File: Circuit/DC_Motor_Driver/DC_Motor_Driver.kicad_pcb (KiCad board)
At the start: 2 copper layers, 54.4 x 18.8 mm, 13 parts, among them Q1 S8050, Q2 S8050, Q3 S8550, Q4 S8050, Q5 IRF540N

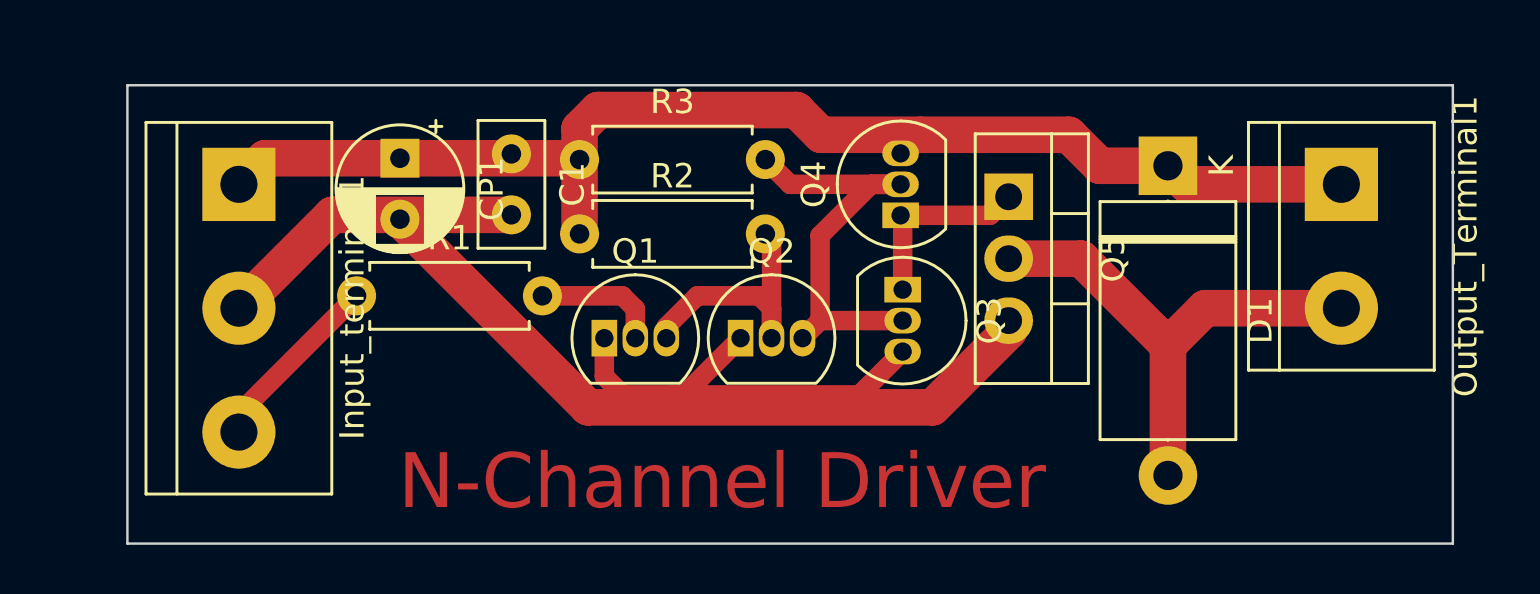
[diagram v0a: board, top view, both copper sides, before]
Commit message: Fixed DC Motor Circuit and discovered fatal design flaw in PWM demultiplexer
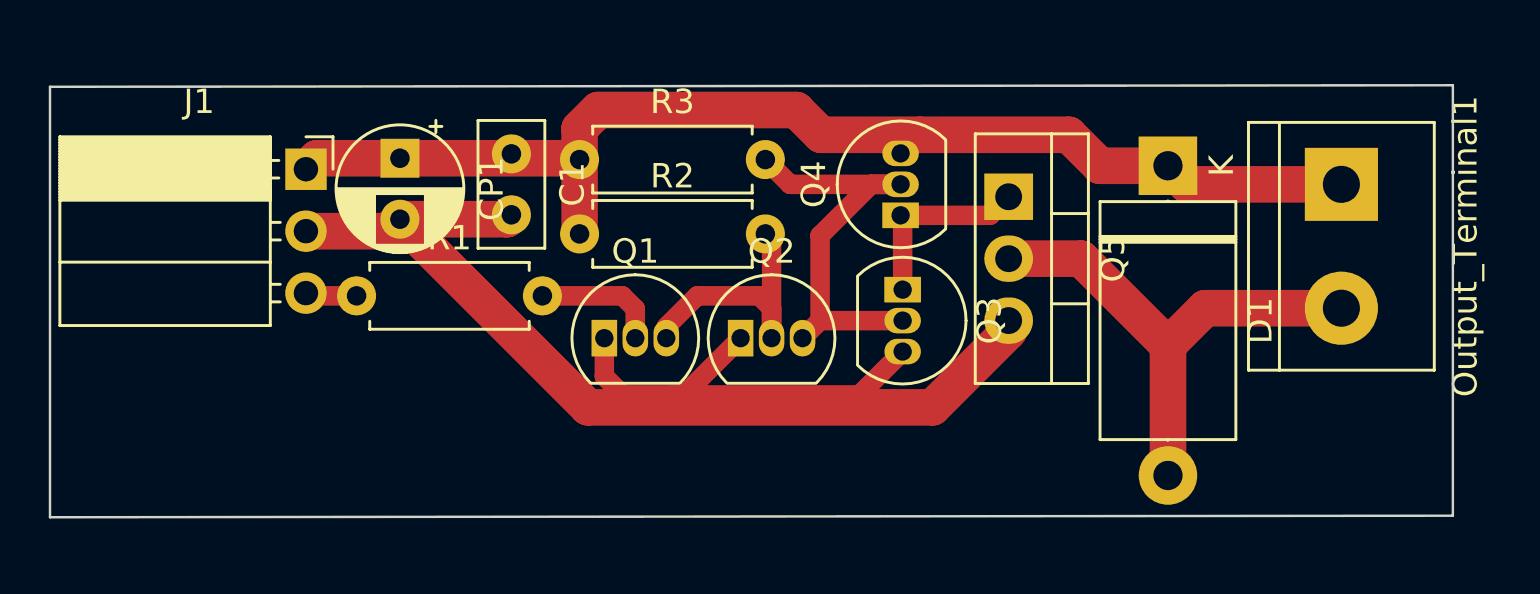
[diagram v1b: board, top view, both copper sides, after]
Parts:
- removed Input_terminal1: Screw_Terminal_01x03, TerminalBlock:TerminalBlock_bornier-3_P5.08mm
- added J1: Conn_01x03_Socket, Connector_PinSocket_2.54mm:PinSocket_1x03_P2.54mm_Horizontal, F.Cu at (20.5, -16.9)
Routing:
- net Control_Signal: track 7.59 -> 2.12 mm
- net GND: track 61.3 -> 57.2 mm
- net +12V: track 52.7 -> 49.7 mm
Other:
- board size 54.4 x 18.8 mm -> 57.5 x 17.7 mm
- board text removed: "N-Channel Driver"

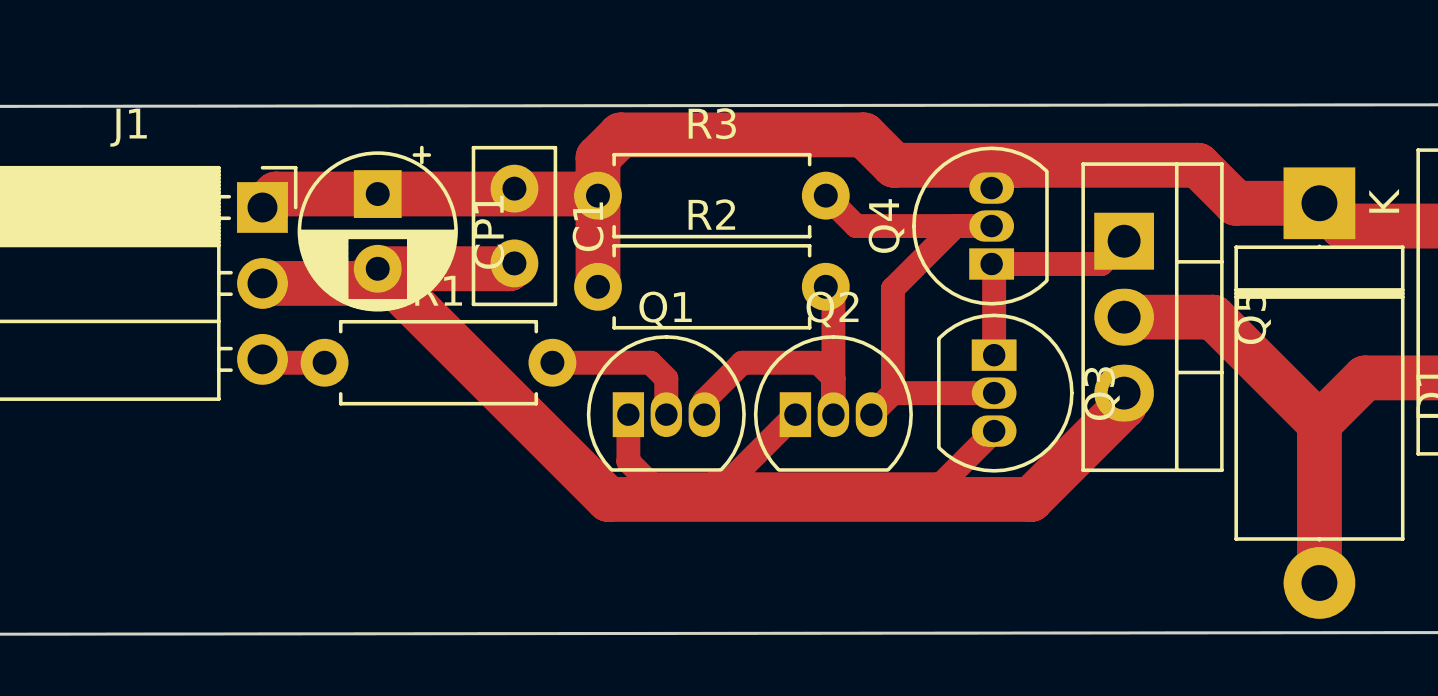
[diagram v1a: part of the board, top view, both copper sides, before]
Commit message: Implemented Isolators in PWM Mutliplexer
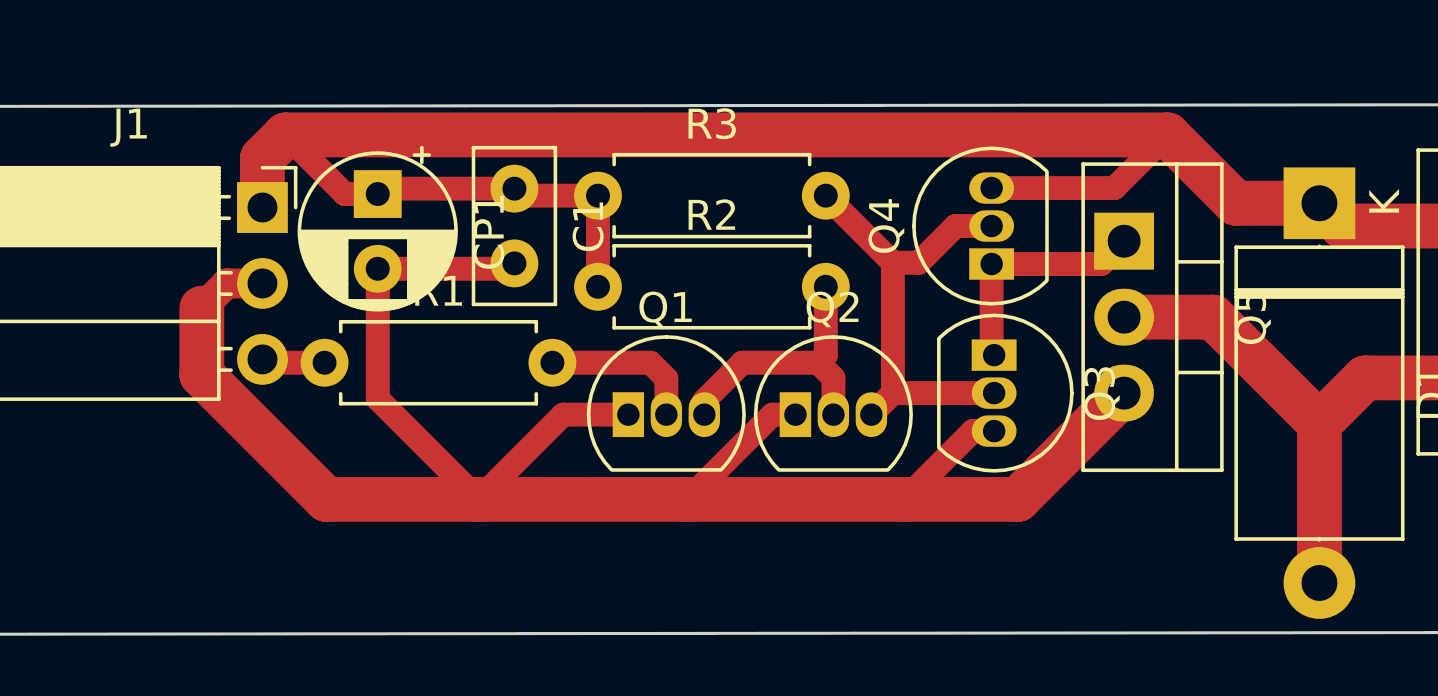
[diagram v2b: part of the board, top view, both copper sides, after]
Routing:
- net +12V: track 49.7 -> 67.2 mm
- net GND: track 57.2 -> 67.3 mm
- net Net-(Q2-C): track 18.0 -> 15.7 mm
- net Net-(Q1-C): track 11.1 -> 9.39 mm
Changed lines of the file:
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@@
   (gr_line (start 10.033 -2.6035) (end 10.033 -20.2565)
     (stroke (width 0.1) (type solid)) (layer "Edge.Cuts"))
-  (segment (start 53.086 -17.018) (end 51.816 -18.288) (width 1.5) (layer "F.Cu") (net 1))
-  (segment (start 31.75 -17.272) (end 31.75 -14.224) (width 1.5) (layer "F.Cu") (net 1))
-  (segment (start 44.916 -17.526) (end 44.958 -17.526) (width 0.8) (layer "F.Cu") (net 1))
-  (segment (start 31.75 -18.542) (end 31.75 -17.272) (width 1.5) (layer "F.Cu") (net 1))
-  (segment (start 51.816 -18.288) (end 45.72 -18.288) (width 1.5) (layer "F.Cu") (net 1))
-  (segment (start 40.64 -19.304) (end 32.512 -19.304) (width 1.5) (layer "F.Cu") (net 1))
-  (segment (start 44.958 -17.526) (end 45.72 -18.288) (width 0.8) (layer "F.Cu") (net 1))
-  (segment (start 24.384 -17.326448) (end 31.695552 -17.326448) (width 1.5) (layer "F.Cu") (net 1))
+  (segment (start 50.8 -19.304) (end 21.304 -19.304) (width 1.5) (layer "F.Cu") (net 1))
+  (segment (start 28.956 -17.506) (end 24.563552 -17.506) (width 0.8) (layer "F.Cu") (net 1))
+  (segment (start 24.563552 -17.506) (end 24.384 -17.326448) (width 0.8) (layer "F.Cu") (net 1))
+  (segment (start 44.916 -17.526) (end 44.778 -17.526) (width 0.8) (layer "F.Cu") (net 1))
+  (segment (start 44.916 -17.526) (end 49.022 -17.526) (width 0.8) (layer "F.Cu") (net 1))
+  (segment (start 31.75 -14.224) (end 31.75 -17.272) (width 0.8) (layer "F.Cu") (net 1))
   (segment (start 62.992 -16.256) (end 56.642 -16.256) (width 1.5) (layer "F.Cu") (net 1))
-  (segment (start 41.656 -18.288) (end 40.64 -19.304) (width 1.5) (layer "F.Cu") (net 1))
-  (segment (start 45.72 -18.288) (end 41.656 -18.288) (width 1.5) (layer "F.Cu") (net 1))
+  (segment (start 28.776448 -17.326448) (end 28.956 -17.506) (width 0.8) (layer "F.Cu") (net 1))
+  (segment (start 24.384 -17.326448) (end 23.281552 -17.326448) (width 0.8) (layer "F.Cu") (net 1))
+  (segment (start 55.88 -17.018) (end 53.086 -17.018) (width 1.5) (layer "F.Cu") (net 1))
+  (segment (start 23.281552 -17.326448) (end 21.304 -19.304) (width 0.8) (layer "F.Cu") (net 1))
+  (segment (start 31.75 -17.272) (end 29.19 -17.272) (width 0.8) (layer "F.Cu") (net 1))
+  (segment (start 49.022 -17.526) (end 50.8 -19.304) (width 0.8) (layer "F.Cu") (net 1))
   (segment (start 56.642 -16.256) (end 55.88 -17.018) (width 1.5) (layer "F.Cu") (net 1))
-  (segment (start 55.88 -17.018) (end 53.086 -17.018) (width 1.5) (layer "F.Cu") (net 1))
-  (segment (start 20.979448 -17.326448) (end 20.529 -16.876) (width 1.5) (layer "F.Cu") (net 1))
-  (segment (start 24.384 -17.326448) (end 20.979448 -17.326448) (width 1.5) (layer "F.Cu") (net 1))
-  (segment (start 31.695552 -17.326448) (end 31.75 -17.272) (width 1.5) (layer "F.Cu") (net 1))
-  (segment (start 32.512 -19.304) (end 31.75 -18.542) (width 1.5) (layer "F.Cu") (net 1))
-  (segment (start 43.222 -7.62) (end 45 -9.398) (width 0.8) (layer "F.Cu") (net 2))
-  (segment (start 23.893552 -14.336) (end 24.384 -14.826448) (width 1.5) (layer "F.Cu") (net 2))
-  (segment (start 28.776448 -14.826448) (end 28.956 -15.006) (width 1.5) (layer "F.Cu") (net 2))
-  (segment (start 32.766 -9.948) (end 32.766 -8.382) (width 0.8) (layer "F.Cu") (net 2))
-  (segment (start 24.384 -14.826448) (end 32.098448 -7.112) (width 1.5) (layer "F.Cu") (net 2))
-  (segment (start 35.56 -7.62) (end 36.026 -7.62) (width 0.8) (layer "F.Cu") (net 2))
-  (segment (start 36.026 -7.62) (end 38.354 -9.948) (width 0.8) (layer "F.Cu") (net 2))
-  (segment (start 33.528 -7.62) (end 35.56 -7.62) (width 0.8) (layer "F.Cu") (net 2))
-  (segment (start 46.228 -7.112) (end 49.347 -10.231) (width 1.5) (layer "F.Cu") (net 2))
-  (segment (start 32.766 -8.382) (end 33.528 -7.62) (width 0.8) (layer "F.Cu") (net 2))
-  (segment (start 49.347 -10.231) (end 49.347 -10.668) (width 1.5) (layer "F.Cu") (net 2))
-  (segment (start 32.098448 -7.112) (end 46.228 -7.112) (width 1.5) (layer "F.Cu") (net 2))
-  (segment (start 24.384 -14.826448) (end 28.776448 -14.826448) (width 1.5) (layer "F.Cu") (net 2))
-  (segment (start 20.529 -14.336) (end 23.893552 -14.336) (width 1.5) (layer "F.Cu") (net 2))
-  (segment (start 35.56 -7.62) (end 43.222 -7.62) (width 0.8) (layer "F.Cu") (net 2))
+  (segment (start 29.19 -17.272) (end 28.956 -17.506) (width 0.8) (layer "F.Cu") (net 1))
+  (segment (start 20.529 -16.876) (end 20.529 -18.529) (width 1.5) (layer "F.Cu") (net 1))
+  (segment (start 20.529 -18.529) (end 21.304 -19.304) (width 1.5) (layer "F.Cu") (net 1))
+  (segment (start 53.086 -17.018) (end 50.8 -19.304) (width 1.5) (layer "F.Cu") (net 1))
+  (segment (start 30.586 -9.948) (end 27.75 -7.112) (width 0.8) (layer "F.Cu") (net 2))
+  (segment (start 49.347 -10.668) (end 45.791 -7.112) (width 1.5) (layer "F.Cu") (net 2))
+  (segment (start 22.667415 -7.112) (end 27.75 -7.112) (width 1.5) (layer "F.Cu") (net 2))
+  (segment (start 18.5 -13.509081) (end 18.5 -11.279415) (width 1.5) (layer "F.Cu") (net 2))
+  (segment (start 27.75 -7.112) (end 34.75 -7.112) (width 1.5) (layer "F.Cu") (net 2))
+  (segment (start 45.791 -7.112) (end 42 -7.112) (width 1.5) (layer "F.Cu") (net 2))
+  (segment (start 44.286 -9.398) (end 45 -9.398) (width 0.8) (layer "F.Cu") (net 2))
+  (segment (start 37.586 -9.948) (end 38.354 -9.948) (width 0.8) (layer "F.Cu") (net 2))
+  (segment (start 24.384 -14.826448) (end 24.384 -10.478) (width 0.8) (layer "F.Cu") (net 2))
+  (segment (start 19.326919 -14.336) (end 18.5 -13.509081) (width 1) (layer "F.Cu") (net 2))
+  (segment (start 34.75 -7.112) (end 42 -7.112) (width 1.5) (layer "F.Cu") (net 2))
+  (segment (start 32.766 -9.948) (end 30.586 -9.948) (width 0.8) (layer "F.Cu") (net 2))
+  (segment (start 18.5 -11.279415) (end 22.667415 -7.112) (width 1.5) (layer "F.Cu") (net 2))
+  (segment (start 44.286 -9.398) (end 42 -7.112) (width 0.8) (layer "F.Cu") (net 2))
+  (segment (start 20.529 -14.336) (end 19.326919 -14.336) (width 1) (layer "F.Cu") (net 2))
+  (segment (start 37.586 -9.948) (end 34.75 -7.112) (width 0.8) (layer "F.Cu") (net 2))
+  (segment (start 28.776448 -14.826448) (end 28.956 -15.006) (width 0.8) (layer "F.Cu") (net 2))
+  (segment (start 24.384 -10.478) (end 27.75 -7.112) (width 0.8) (layer "F.Cu") (net 2))
+  (segment (start 24.384 -14.826448) (end 28.776448 -14.826448) (width 0.8) (layer "F.Cu") (net 2))
   (segment (start 55.88 -9.652) (end 55.88 -4.318) (width 1.5) (layer "F.Cu") (net 3))
   (segment (start 57.404 -11.176) (end 62.992 -11.176) (width 1.5) (layer "F.Cu") (net 3))
@@
   (segment (start 52.324 -13.208) (end 55.88 -9.652) (width 1.5) (layer "F.Cu") (net 3))
   (segment (start 55.88 -9.652) (end 57.404 -11.176) (width 1.5) (layer "F.Cu") (net 3))
+  (segment (start 34.036 -9.948) (end 34.036 -11.153) (width 0.8) (layer "F.Cu") (net 4))
   (segment (start 33.505 -11.684) (end 34.036 -11.153) (width 0.8) (layer "F.Cu") (net 4))
-  (segment (start 34.036 -11.153) (end 34.036 -9.948) (width 0.8) (layer "F.Cu") (net 4))
   (segment (start 30.226 -11.684) (end 33.505 -11.684) (width 0.8) (layer "F.Cu") (net 4))
+  (segment (start 39.37 -11.938) (end 39.37 -14.224) (width 0.8) (layer "F.Cu") (net 5))
   (segment (start 39.624 -11.176) (end 39.624 -9.948) (width 0.8) (layer "F.Cu") (net 5))
-  (segment (start 39.624 -9.948) (end 39.624 -13.97) (width 0.8) (layer "F.Cu") (net 5))
   (segment (start 35.306 -10.414) (end 36.576 -11.684) (width 0.8) (layer "F.Cu") (net 5))
+  (segment (start 36.576 -11.684) (end 39.116 -11.684) (width 0.8) (layer "F.Cu") (net 5))
+  (segment (start 39.116 -11.684) (end 39.624 -11.176) (width 0.8) (layer "F.Cu") (net 5))
+  (segment (start 39.37 -11.938) (end 39.116 -11.684) (width 0.8) (layer "F.Cu") (net 5))
   (segment (start 35.306 -9.948) (end 35.306 -10.414) (width 0.8) (layer "F.Cu") (net 5))
-  (segment (start 36.576 -11.684) (end 39.116 -11.684) (width 0.8) (layer "F.Cu") (net 5))
-  (segment (start 39.624 -13.97) (end 39.37 -14.224) (width 0.8) (layer "F.Cu") (net 5))
-  (segment (start 39.116 -11.684) (end 39.624 -11.176) (width 0.8) (layer "F.Cu") (net 5))
+  (segment (start 41.614 -10.668) (end 41.614 -15.028) (width 0.8) (layer "F.Cu") (net 6))
+  (segment (start 41.614 -15.028) (end 39.37 -17.272) (width 0.8) (layer "F.Cu") (net 6))
   (segment (start 43.711 -16.256) (end 44.916 -16.256) (width 0.8) (layer "F.Cu") (net 6))
-  (segment (start 41.614 -14.159) (end 43.711 -16.256) (width 0.8) (layer "F.Cu") (net 6))
-  (segment (start 40.386 -16.256) (end 44.916 -16.256) (width 0.8) (layer "F.Cu") (net 6))
   (segment (start 40.894 -9.948) (end 41.614 -10.668) (width 0.8) (layer "F.Cu") (net 6))
-  (segment (start 39.37 -17.272) (end 40.386 -16.256) (width 0.8) (layer "F.Cu") (net 6))
   (segment (start 41.614 -10.668) (end 45 -10.668) (width 0.8) (layer "F.Cu") (net 6))
-  (segment (start 41.614 -10.668) (end 41.614 -14.159) (width 0.8) (layer "F.Cu") (net 6))
-  (segment (start 45 -11.938) (end 45 -14.902) (width 0.8) (layer "F.Cu") (net 7))
+  (segment (start 41.614 -15.028) (end 42.483 -15.028) (width 0.8) (layer "F.Cu") (net 6))
+  (segment (start 42.483 -15.028) (end 43.711 -16.256) (width 0.8) (layer "F.Cu") (net 6))
+  (segment (start 44.916 -14.986) (end 44.916 -12.022) (width 0.8) (layer "F.Cu") (net 7))
   (segment (start 48.585 -14.986) (end 49.347 -15.748) (width 0.8) (layer "F.Cu") (net 7))
-  (segment (start 45 -14.902) (end 44.916 -14.986) (width 0.8) (layer "F.Cu") (net 7))
+  (segment (start 44.916 -12.022) (end 45 -11.938) (width 0.8) (layer "F.Cu") (net 7))
   (segment (start 44.916 -14.986) (end 48.585 -14.986) (width 0.8) (layer "F.Cu") (net 7))
   (segment (start 22.606 -11.684) (end 20.641 -11.684) (width 0.8) (layer "F.Cu") (net 8))
